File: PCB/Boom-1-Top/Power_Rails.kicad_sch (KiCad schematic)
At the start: 47 parts, among them J19 3V3 Bypass, J20 5V Bypass, J54 OLEDPowerTest, Q1 AO3401A, Q2 AO3401A, U21 MP2359DJ-LF-Z, U42 MP2359DJ-LF-Z, U54 MP1541

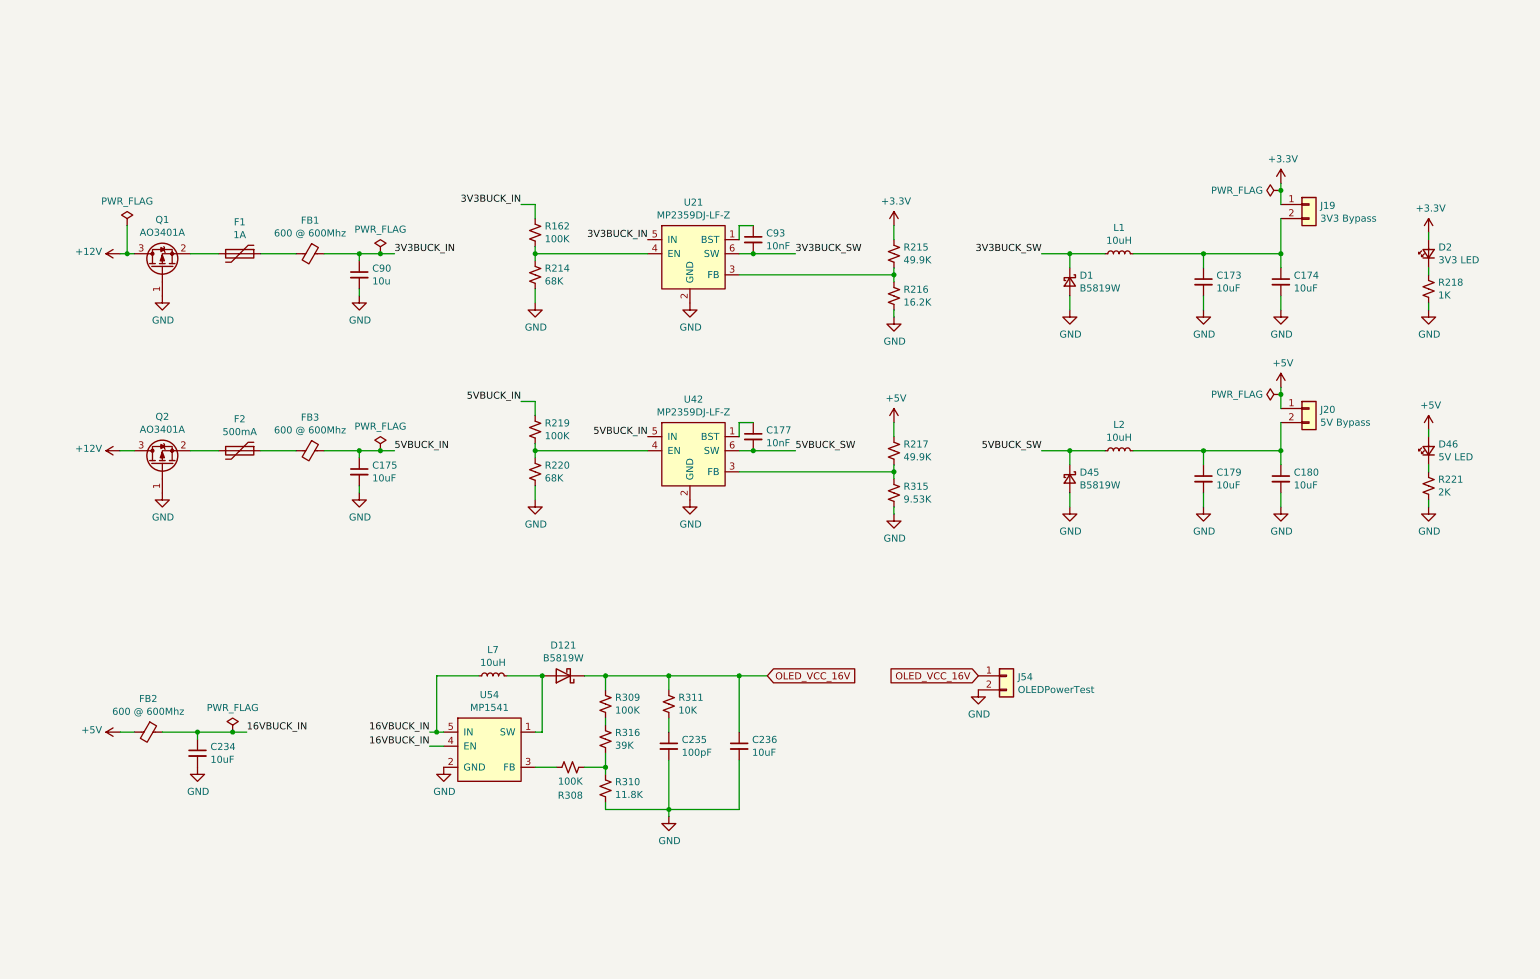
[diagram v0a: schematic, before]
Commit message: Top: moved power connectors to Power Rails; moved anything pertaining to DACs into DACs
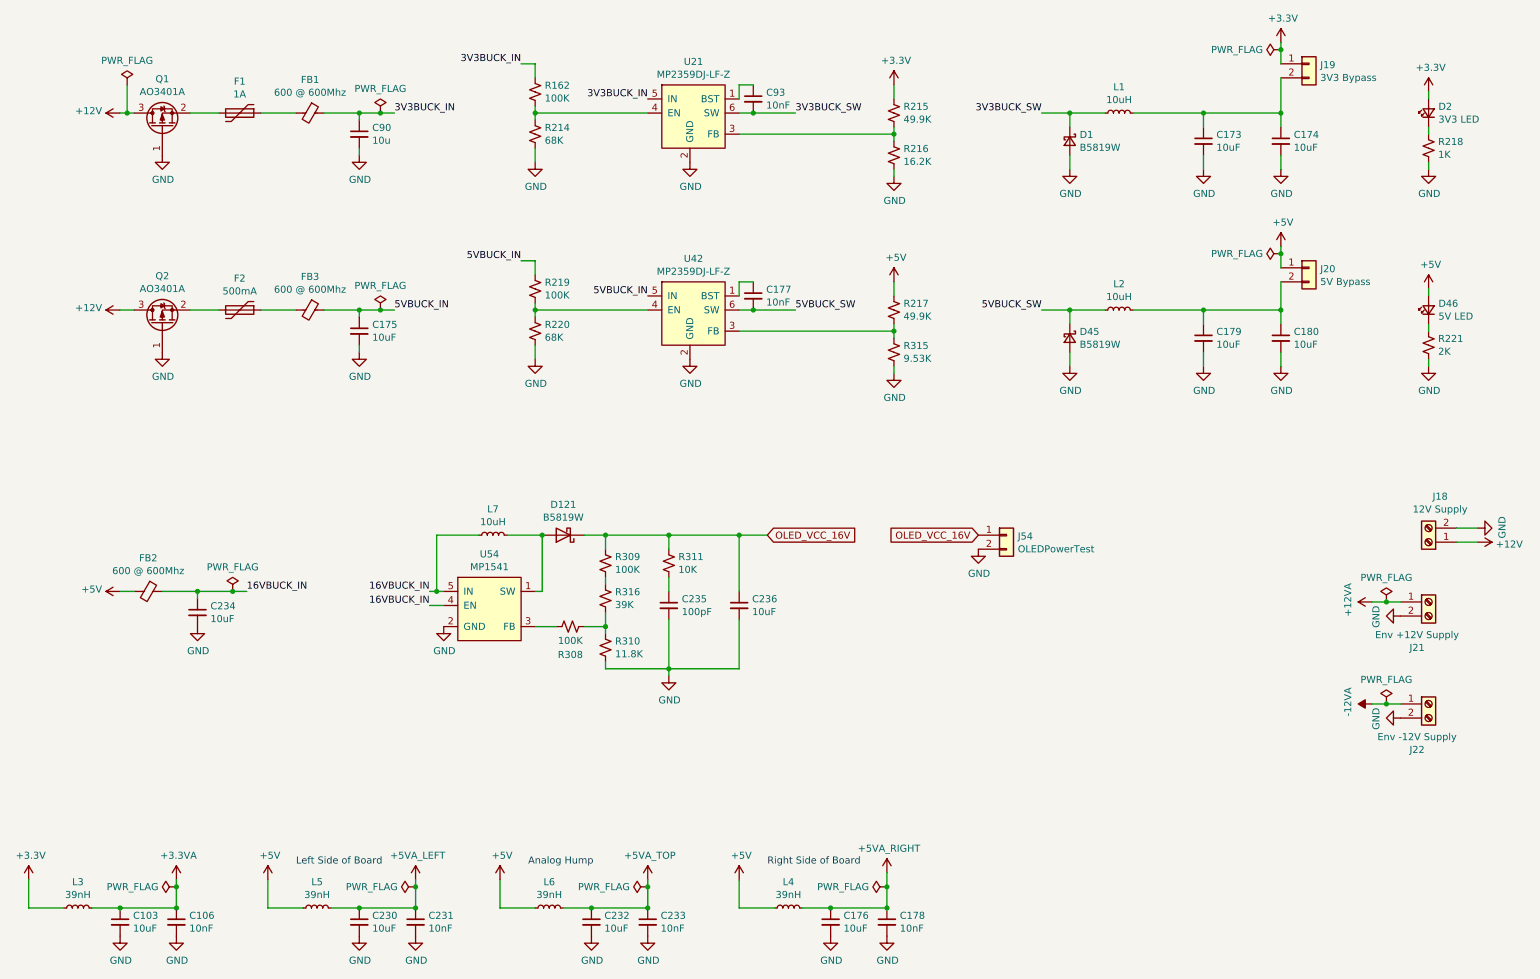
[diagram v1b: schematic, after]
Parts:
- added C103, C176, C230, C232: 10uF, Capacitor_SMD:C_1206_3216Metric, symbol Device:C_Small
- added C106, C178, C231, C233: 10nF, Capacitor_SMD:C_0402_1005Metric, symbol Device:C_Small
- added J18: 12V Supply, TerminalBlock:TerminalBlock_bornier-2_P5.08mm, symbol Connector:Screw_Terminal_01x02
- added J21: Env +12V Supply, TerminalBlock:TerminalBlock_bornier-2_P5.08mm, symbol Connector:Screw_Terminal_01x02
- added J22: Env -12V Supply, TerminalBlock:TerminalBlock_bornier-2_P5.08mm, symbol Connector:Screw_Terminal_01x02
- added L3, L4, L5, L6: 39nH, Inductor_SMD:L_0402_1005Metric, symbol Device:L_Small
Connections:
- net +12V: now also J18.1 (Pin_1)
- net +3V3: now also L3.1
- net +5V: now also L4.1, L5.1, L6.1
- net GND: now also C103.2, C106.2, C176.2, C178.2, C230.2, C231.2, C232.2, C233.2, J18.2 (Pin_2), J21.2 (Pin_2), J22.2 (Pin_2)
- new net +12VA: J21.1 (Pin_1)
- new net +3.3VA: C103.1, C106.1, L3.2
- new net +5VA_LEFT: C230.1, C231.1, L5.2
- new net +5VA_RIGHT: C176.1, C178.1, L4.2
- new net +5VA_TOP: C232.1, C233.1, L6.2
- new net -12VA: J22.1 (Pin_1)
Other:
- note added: "Analog Hump"
- note added: "Left Side of Board"
- note added: "Right Side of Board"
- moved on the sheet: C173, C174, C175, C177, C179, C180, C234, C235, C236, C90, C93, D1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
